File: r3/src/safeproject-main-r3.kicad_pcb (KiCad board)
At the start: 4 copper layers, 57.3 x 109 mm, 150 parts, among them J1 , J10 Conn_01x05_MountingPin, J11 SMA, J12 U_FL-R-SMT-1_10_, J13 JAE_SIM_Card_SF72S006, J14 Micro_SD_Card_Det_JAE_ST11, J15 10118194, J16 FH12A-20S-0.5SH, J2 , J3 , J4 , J5 , J6 , J7 , J8 , J9 , Q1 Si7113ADN, Q2 Si7113ADN, Q3 Si7113ADN, Q4 NX3008NBKW, T1 , T10 , T11 , T3 , T4 , T5 , T6 , T7 , T8 , T9 , U1 74LVC1G07DCK, U10 ESD7004, U11 ESD7004, U12 CP2102N-Axx-xQFN24, U13 DS3231MZ, U14 74LVC1G07DCK, U15 FSUSB42MX, U16 ESD7004, U17 PCA9685PW, U2 ESD7004, U3 DZDH0401DW, U4 DZDH0401DW, U5 LM60440DRPK, U6 LM60440DRPK, U7 Sierra_Wireless_RC7620, U8 ESD7004, U9 TXS0108EPW

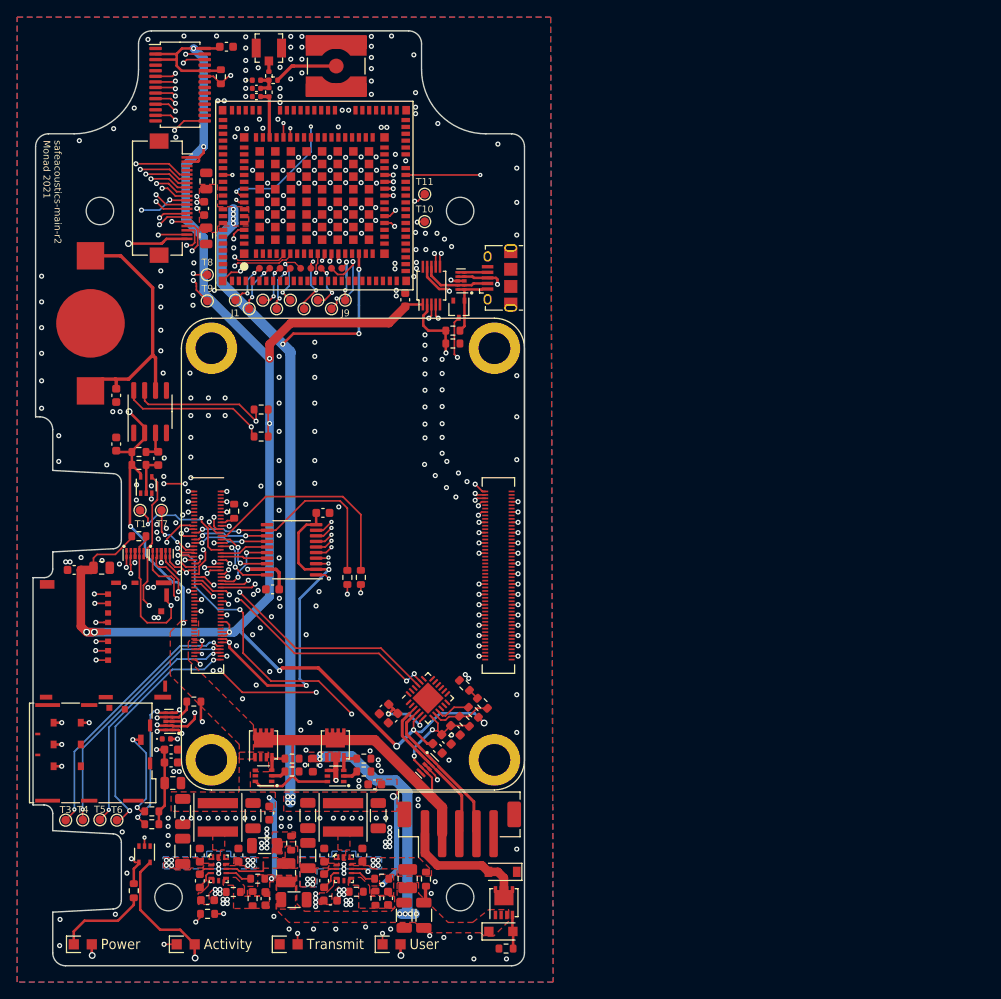
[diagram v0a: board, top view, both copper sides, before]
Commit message: Most of the new level translator circuit routed. Add new test points
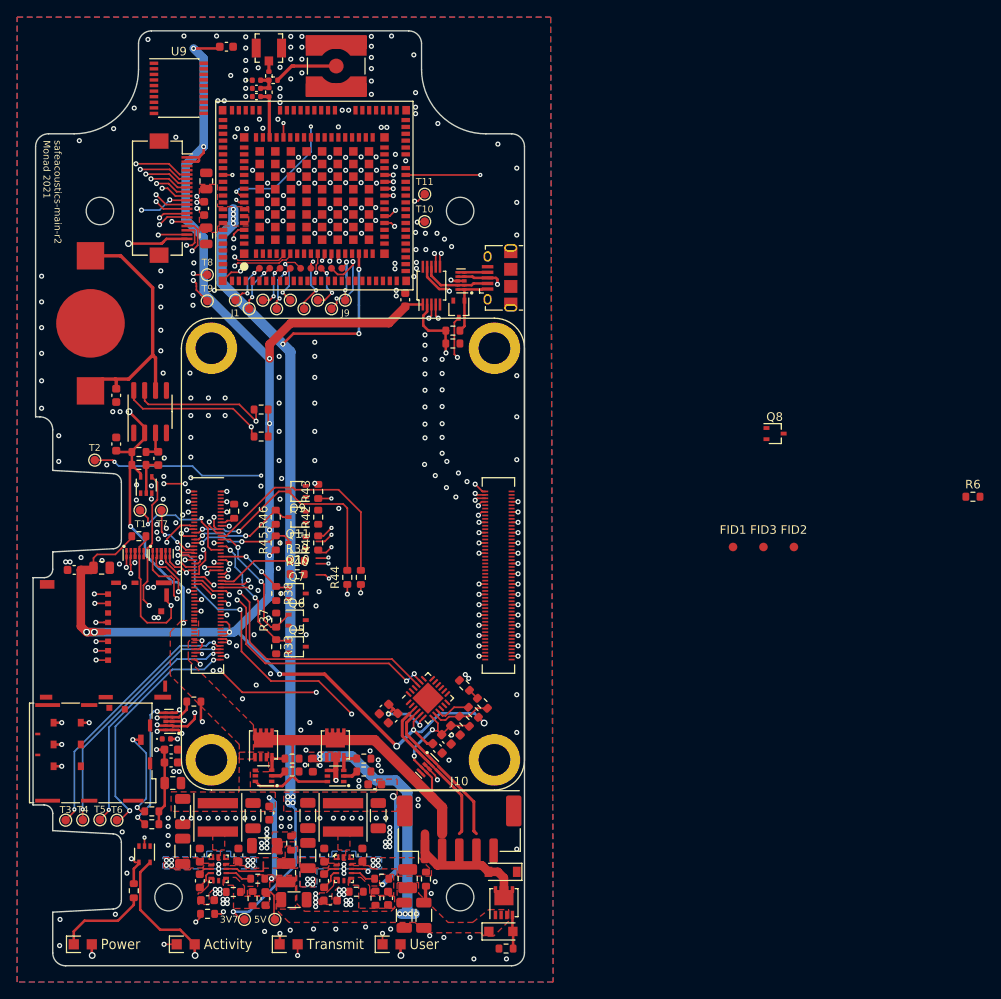
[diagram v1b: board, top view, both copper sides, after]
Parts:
- removed C25, C27: 100nF, Capacitor_SMD:C_0603_1608Metric
- removed U17: PCA9685PW, Package_SO:TSSOP-28_4.4x9.7mm_P0.65mm
- added 3V7: , TestPoint:TestPoint_Pad_D1.0mm, F.Cu at (-4.15, 42.6)
- added 5V: , TestPoint:TestPoint_Pad_D1.0mm, F.Cu at (-0.60, 42.6)
- added FID1: Fiducial, Fiducial:Fiducial_1mm_Mask2mm, F.Cu at (52.8, -0.82)
- added FID2: Fiducial, Fiducial:Fiducial_1mm_Mask2mm, F.Cu at (59.9, -0.82)
- added FID3: Fiducial, Fiducial:Fiducial_1mm_Mask2mm, F.Cu at (56.4, -0.82)
- added Q10: NX3008NBKW, Package_TO_SOT_SMD:SOT-323_SC-70, F.Cu at (2.00, -1.30)
- added Q11: NX3008NBKW, Package_TO_SOT_SMD:SOT-323_SC-70, F.Cu at (2.00, -4.30)
- added Q5: NX3008NBKW, Package_TO_SOT_SMD:SOT-323_SC-70, F.Cu at (2.00, 10.8)
- added Q6: NX3008NBKW, Package_TO_SOT_SMD:SOT-323_SC-70, F.Cu at (2.00, 7.70)
- added Q7: NX3008NBKW, Package_TO_SOT_SMD:SOT-323_SC-70, F.Cu at (2.00, 4.60)
- added Q8: NX3008NBKW, Package_TO_SOT_SMD:SOT-323_SC-70, F.Cu at (57.7, -14.0)
- added Q9: NX3008NBKW, Package_TO_SOT_SMD:SOT-323_SC-70, F.Cu at (2.00, -7.30)
- added R37: 10k, Resistor_SMD:R_0603_1608Metric, F.Cu at (-0.45, 7.70)
- added R38: 10k, Resistor_SMD:R_0603_1608Metric, F.Cu at (-0.45, 4.60)
- added R39: 10k, Resistor_SMD:R_0603_1608Metric, F.Cu at (2.00, 0.80)
- added R40: 10k, Resistor_SMD:R_0603_1608Metric, F.Cu at (2.00, 2.35)
- added R41: 10k, Resistor_SMD:R_0603_1608Metric, F.Cu at (4.45, -1.30)
- added R42: 10k, Resistor_SMD:R_0603_1608Metric, F.Cu at (4.45, -4.30)
- added R43: 10k, Resistor_SMD:R_0603_1608Metric, F.Cu at (4.45, -7.30)
- added R44: 1k, Resistor_SMD:R_0603_1608Metric, F.Cu at (7.84, 2.72)
- added R45: 10k, Resistor_SMD:R_0603_1608Metric, F.Cu at (-0.50, -1.30)
- added R46: 10k, Resistor_SMD:R_0603_1608Metric, F.Cu at (-0.50, -4.30)
- added T2: , TestPoint:TestPoint_Pad_D1.0mm, F.Cu at (-21.6, -10.9)
- J10: value Conn_01x05_MountingPin -> 502443-0560; footprint Connector_JST:JST_PH_B5B-PH-SM4-TB_1x05-1MP_P2.00mm_Vertical -> Connector_Molex:Molex_CLIK-Mate_502443-0570_1x05-1MP_P2.00mm_Vertical
- R21: value DNP 29.4k -> 10k
- R33: value 100k -> 10k
- R6: value 1k -> 10k
- U9: value TXS0108EPW -> PCF8574PW; footprint Package_SO:TSSOP-20_4.4x6.5mm_P0.65mm -> Package_SO:SSOP-20_4.4x6.5mm_P0.65mm
- moved R6 73.5 mm to (80.8, -6.68), turned to 0 degrees
- moved R33 66.8 mm to (-0.45, 10.8), turned to -90 degrees
- moved U9 55.4 mm to (-11.8, -54.3), turned to 0 degrees
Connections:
- D3 pad 1: GND -> Net-(D3-Pad1)
- D3 pad 2: Net-(D3-Pad2) -> +3V3
- D6 pad 2: /Modem/UIM_SIM_DET -> Net-(D6-Pad2)
- J13 pad C7: /Modem/UIM_DATA -> /Modem/UIM_CLK
- J13 pad DSW: /Modem/UIM_SIM_DET -> Net-(D6-Pad2)
- Module1 pad 44: /nLEDS_ENABLE -> unconnected-(Module1-Pad44)
- Module1 pad 88: +1V8 -> /+1V8
- Module1 pad 90: +1V8 -> /+1V8
- R21 pad 1: /Modem/UIM_SIM_DET -> Net-(D6-Pad2)
- R22 pad 1: /Modem/UIM_DATA -> /Modem/UIM_CLK
- R33 pad 1: /nLEDS_ENABLE -> /POWER_ON_N
- R33 pad 2: +3V3 -> GND
- R6 pad 1: /TX_ON -> /3V7_EN
- R6 pad 2: Net-(D3-Pad2) -> GND
- U7 pad 28: /Modem/UIM_DATA -> /Modem/UIM_CLK
- U7 pad 46: /Modem/1V8_RESET_OUT_N -> unconnected-(U7-Pad46)
- U8 pad 5: /Modem/UIM_DATA -> /Modem/UIM_CLK
- U9 pad 1: /Modem/1V8_POWER_ON_N -> unconnected-(U9-Pad1)
- U9 pad 10: +1V8 -> /LED driver, LED board connections/LED1_R
- U9 pad 11: GND -> /LED driver, LED board connections/LED1_G
- U9 pad 12: /TX_ON -> /LED driver, LED board connections/LED1_B
- U9 pad 13: /WAKE_ON_WWAN -> unconnected-(U9-Pad13)
- U9 pad 14: /SAFE_PWR_REMOVE -> /LED driver, LED board connections/LED2_R
- U9 pad 15: /RESET_OUT_N -> GND
- U9 pad 16: /WAKE -> /LED driver, LED board connections/LED2_G
- U9 pad 17: /BOOT_MODE -> /LED driver, LED board connections/LED2_B
- U9 pad 18: /RESET_IN_N -> unconnected-(U9-Pad18)
- U9 pad 19: +3V3 -> /LED driver, LED board connections/LED3_G
- U9 pad 2: +1V8 -> /SCL
- U9 pad 20: /POWER_ON_N -> /LED driver, LED board connections/LED3_B
- U9 pad 3: /Modem/1V8_RESET_IN_N -> unconnected-(U9-Pad3)
- U9 pad 4: /Modem/1V8_BOOT_MODE -> /SDA
- U9 pad 5: /Modem/1V8_WAKE -> +3V3
- U9 pad 6: /Modem/1V8_RESET_OUT_N -> +3V3
- U9 pad 7: /Modem/1V8_SAFE_PWR_REMOVE -> +3V3
- U9 pad 8: /Modem/1V8_WAKE_ON_WWAN -> unconnected-(U9-Pad8)
- U9 pad 9: /Modem/1V8_TX_ON -> GND
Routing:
- net /Modem/UIM_DATA: track 107.6 -> 0.00 mm, vias 5 -> 0
- net /Modem/UIM_CLK: track 79.5 -> 187.1 mm, vias 2 -> 7
- net Net-(D6-Pad2): track 0.00 -> 91.4 mm, vias 0 -> 4
- net /Modem/UIM_SIM_DET: track 91.4 -> 0.00 mm, vias 4 -> 0
- net /nLEDS_ENABLE: track 83.1 -> 0.00 mm, vias 4 -> 0
- net /Modem/1V8_RESET_OUT_N: track 81.3 -> 0.00 mm, vias 2 -> 0
- net unconnected-(Module1-Pad44): track 0.00 -> 79.3 mm, vias 0 -> 4
- net Net-(D3-Pad1): track 0.00 -> 45.2 mm, vias 0 -> 2
- net /+1V8: track 0.00 -> 44.4 mm, vias 0 -> 3
- net Net-(D3-Pad2): track 44.4 -> 0.00 mm, vias 2 -> 0
- net +1V8: track 40.1 -> 0.00 mm, vias 3 -> 0
- net +3V3: track 308.3 -> 288.0 mm, vias 15 -> 17
- net +3V7: track 103.4 -> 122.0 mm, vias 13 -> 14
- net VBUS: track 57.3 -> 72.3 mm
- net /Power and input connector/IN_VIN: track 15.0 -> 0.00 mm
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
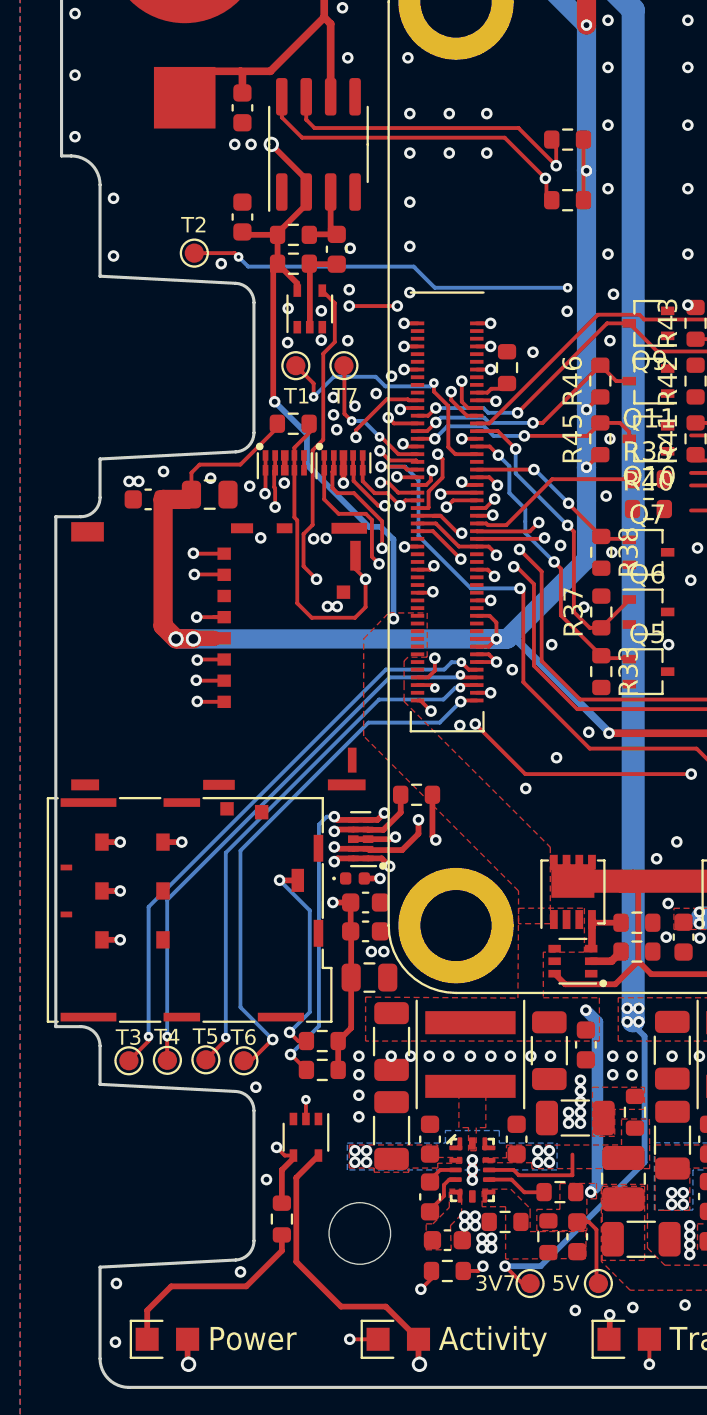
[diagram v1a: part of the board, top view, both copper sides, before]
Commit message: Test points routed
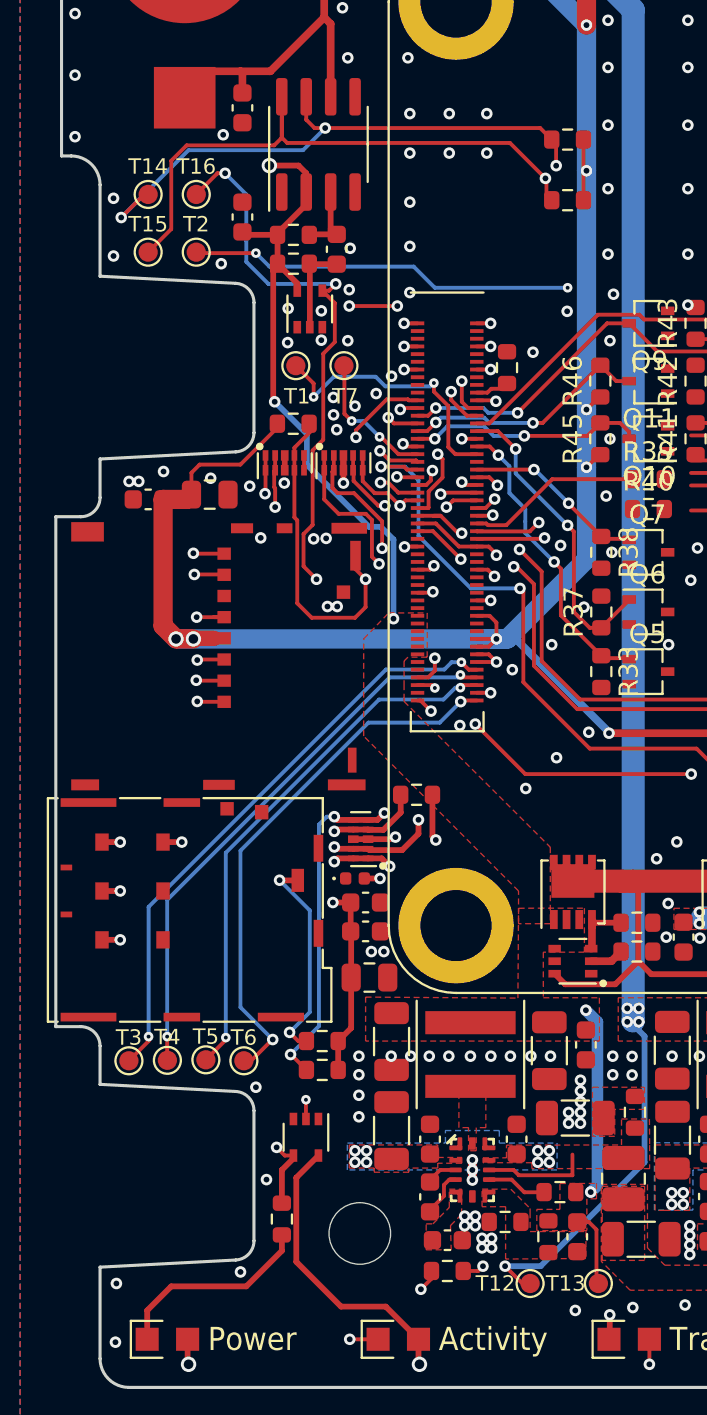
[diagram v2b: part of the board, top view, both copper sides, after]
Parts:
- added T14: , TestPoint:TestPoint_Pad_D1.0mm, F.Cu at (-24.0, -14.0)
- added T15: , TestPoint:TestPoint_Pad_D1.0mm, F.Cu at (-24.0, -11.0)
- added T16: , TestPoint:TestPoint_Pad_D1.0mm, F.Cu at (-21.5, -14.0)
- moved T2 0.11 mm to (-21.5, -11.0)
- renumbered 3V7 to T12, 5V to T13
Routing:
- net /SDA: track 93.6 -> 107.6 mm, vias 3 -> 5
- net /SCL: track 91.8 -> 105.0 mm
- net /GLOBAL_EN_o: track 27.1 -> 40.0 mm, vias 2 -> 4
- net +5V: track 73.7 -> 74.7 mm
- net GND: vias 387 -> 386

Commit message: Level translator routed
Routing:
- net /Modem/1V8_POWER_ON_N: track 87.8 -> 106.9 mm
- net /Modem/1V8_BOOT_MODE: track 74.1 -> 89.1 mm
- net /Modem/1V8_WAKE_ON_WWAN: track 50.9 -> 62.2 mm, vias 1 -> 2
- net /Modem/1V8_SAFE_PWR_REMOVE: track 78.2 -> 89.4 mm
- net /Modem/1V8_RESET_IN_N: track 39.0 -> 44.5 mm
- net /Modem/1V8_WAKE: track 37.1 -> 40.4 mm
- net /Modem/1V8_TX_ON: track 81.0 -> 82.5 mm
